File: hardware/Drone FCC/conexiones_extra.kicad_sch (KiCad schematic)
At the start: 4 parts, among them J1 UARTs externo x 3, J1001 SPI externo, J1003 I2C externo x2, J1005 5V y 3V3 x 2

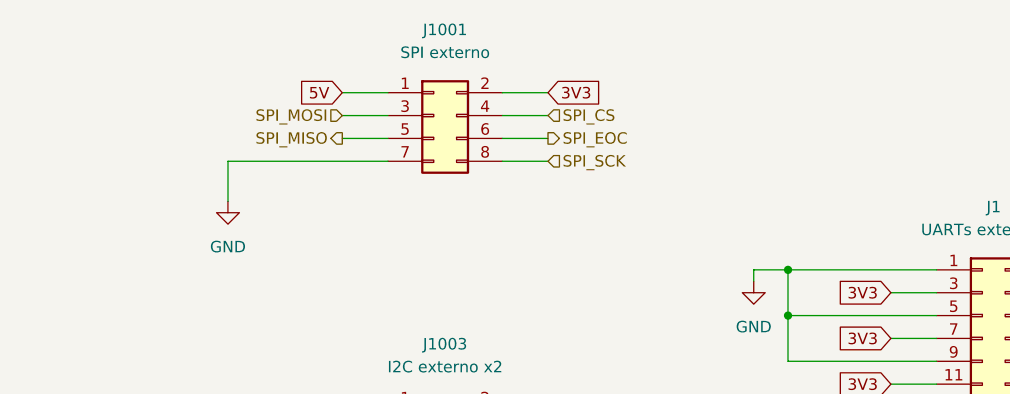
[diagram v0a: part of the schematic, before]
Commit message: add series resistor SPI buses
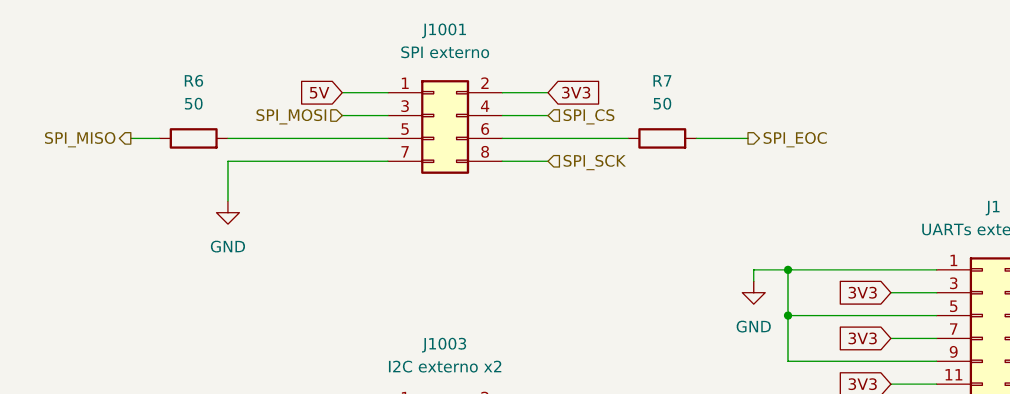
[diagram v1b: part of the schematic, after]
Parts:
- added R6, R7: 50, Resistor_SMD:R_0402_1005Metric_Pad0.72x0.64mm_HandSolder, symbol Device:R
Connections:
- net SPI_EOC: now also R7.2; no longer J1001.6 (Pin_6)
- net SPI_MISO: now also R6.1; no longer J1001.5 (Pin_5)
- new net: J1001.5 (Pin_5), R6.2
- new net: J1001.6 (Pin_6), R7.1
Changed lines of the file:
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@@
     (stroke (width 0) (type default) (color 0 0 0 0))
   )
-  (wire (pts (xy 52.07 35.56) (xy 57.15 35.56))
+  (wire (pts (xy 39.37 35.56) (xy 57.15 35.56))
     (stroke (width 0) (type default) (color 0 0 0 0))
   )
@@
     (stroke (width 0) (type default) (color 0 0 0 0))
   )
+  (wire (pts (xy 91.44 35.56) (xy 97.155 35.56))
+    (stroke (width 0) (type default) (color 0 0 0 0))
+  )
   (wire (pts (xy 57.15 33.02) (xy 52.07 33.02))
     (stroke (width 0) (type default) (color 0 0 0 0))
@@
     (stroke (width 0) (type default) (color 0 0 0 0))
   )
-  (wire (pts (xy 69.85 35.56) (xy 74.93 35.56))
-    (stroke (width 0) (type default) (color 0 0 0 0))
-  )
   (wire (pts (xy 69.85 75.565) (xy 78.74 75.565))
     (stroke (width 0) (type default) (color 0 0 0 0))
   )
+  (wire (pts (xy 69.85 35.56) (xy 83.82 35.56))
+    (stroke (width 0) (type default) (color 0 0 0 0))
+  )
   (wire (pts (xy 101.6 55.245) (xy 118.11 55.245))
     (stroke (width 0) (type default) (color 0 0 0 0))
@@
     (stroke (width 0) (type default) (color 0 0 0 0))
   )
+  (wire (pts (xy 28.575 35.56) (xy 31.75 35.56))
+    (stroke (width 0) (type default) (color 0 0 0 0))
+  )
   (wire (pts (xy 74.93 38.1) (xy 69.85 38.1))
     (stroke (width 0) (type default) (color 0 0 0 0))
@@
     (effects (font (size 1.27 1.27)) (justify right))
   )
-  (hierarchical_label "SPI_EOC" (shape output) (at 74.93 35.56 0)
+  (hierarchical_label "SPI_EOC" (shape output) (at 97.155 35.56 0)
     (effects (font (size 1.27 1.27)) (justify left))
   )
@@
     (effects (font (size 1.27 1.27)) (justify right))
   )
-  (hierarchical_label "SPI_MISO" (shape output) (at 52.07 35.56 180)
+  (hierarchical_label "SPI_MISO" (shape output) (at 28.575 35.56 180)
     (effects (font (size 1.27 1.27)) (justify right))
   )
@@
     (pin "1")
   )
+  (symbol (lib_id "Device:R") (at 87.63 35.56 90) (unit 1)
+    (in_bom yes) (on_board yes) (fields_autoplaced)
+    (property "Reference" "R7" (id 0) (at 87.63 29.21 90))
+    (property "Value" "50" (id 1) (at 87.63 31.75 90))
+    (property "Footprint" "Resistor_SMD:R_0402_1005Metric_Pad0.72x0.64mm_HandSolder" (id 2) (at 87.63 37.338 90)
+      (effects (font (size 1.27 1.27)) hide)
+    )
+    (property "Datasheet" "~" (id 3) (at 87.63 35.56 0)
+      (effects (font (size 1.27 1.27)) hide)
+    )
+    (pin "1")
+    (pin "2")
+  )
+  (symbol (lib_id "Device:R") (at 35.56 35.56 90) (unit 1)
+    (in_bom yes) (on_board yes) (fields_autoplaced)
+    (property "Reference" "R6" (id 0) (at 35.56 29.21 90))
+    (property "Value" "50" (id 1) (at 35.56 31.75 90))
+    (property "Footprint" "Resistor_SMD:R_0402_1005Metric_Pad0.72x0.64mm_HandSolder" (id 2) (at 35.56 37.338 90)
+      (effects (font (size 1.27 1.27)) hide)
+    )
+    (property "Datasheet" "~" (id 3) (at 35.56 35.56 0)
+      (effects (font (size 1.27 1.27)) hide)
+    )
+    (pin "1")
+    (pin "2")
+  )
   (symbol (lib_id "Connector_Generic:Conn_02x06_Odd_Even") (at 123.19 55.245 0) (unit 1)

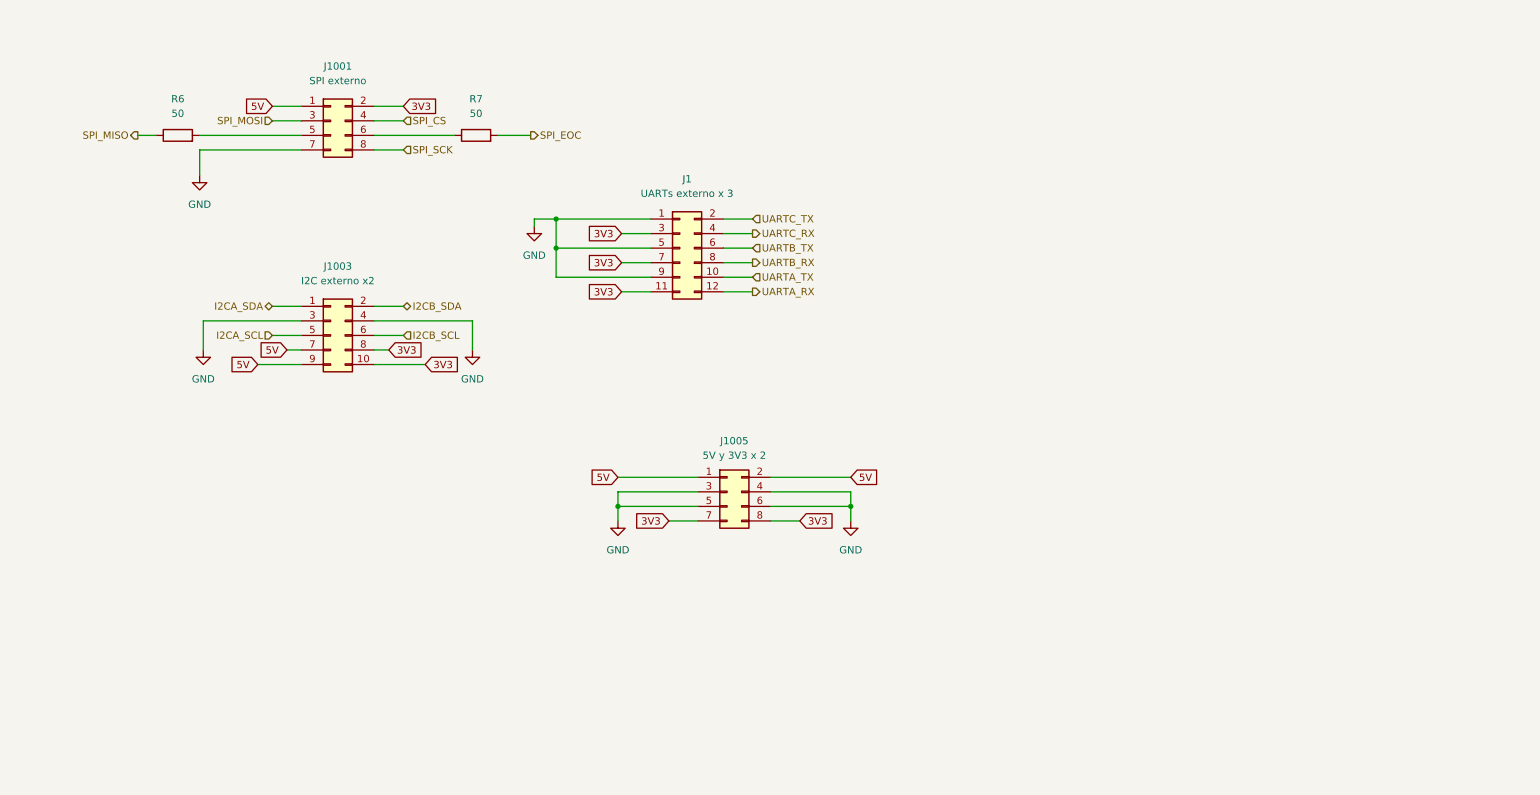
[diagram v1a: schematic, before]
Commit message: add TVS diodes for SPI and ESD capacitors
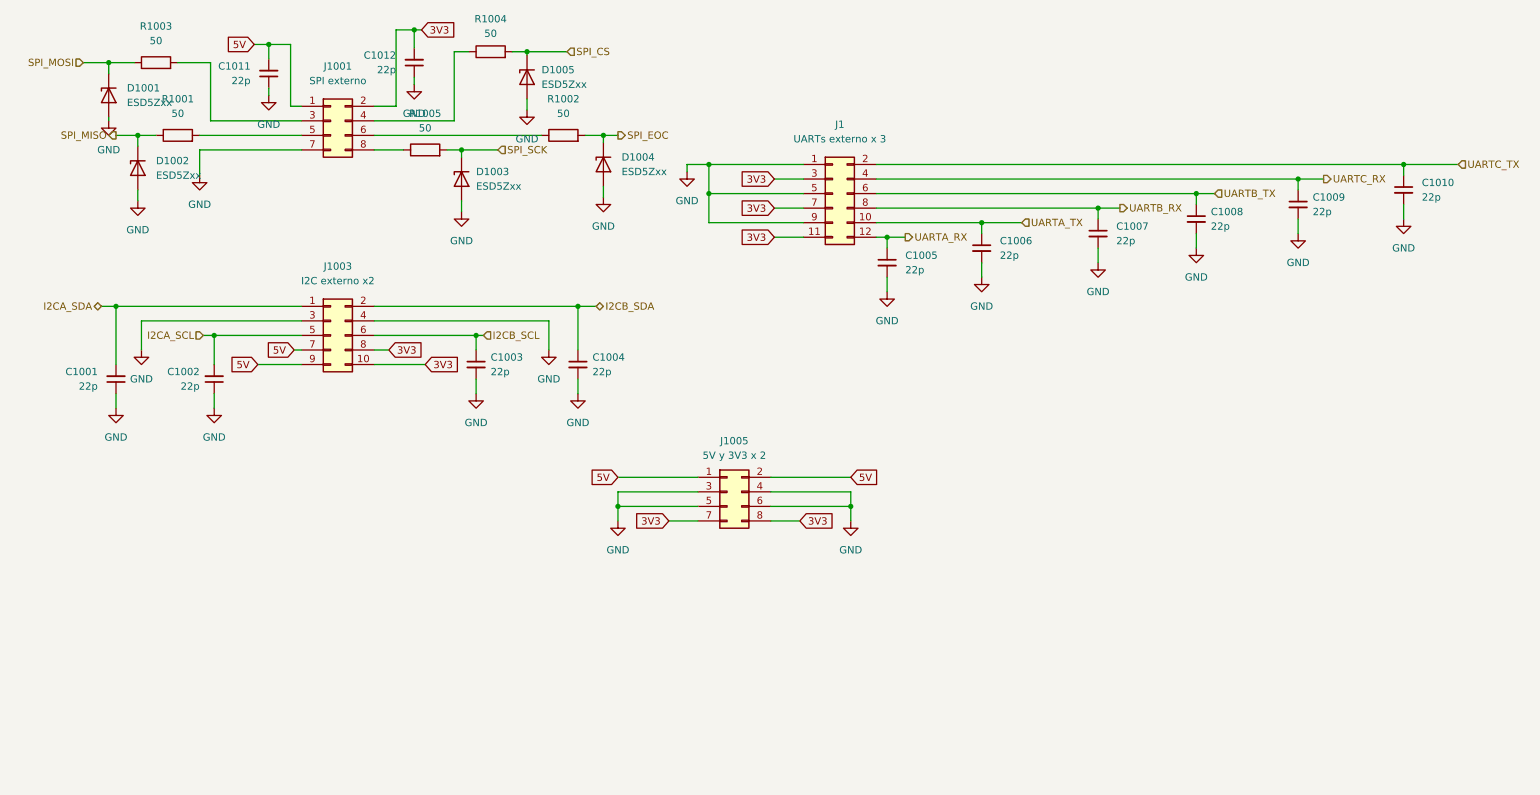
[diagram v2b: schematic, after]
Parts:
- added C1001, C1002, C1003, C1004, C1005, C1006, C1007, C1008, C1009, C1010, C1011, C1012: 22p, Capacitor_SMD:C_0402_1005Metric_Pad0.74x0.62mm_HandSolder, symbol Device:C_Small
- added D1001, D1002, D1003, D1004, D1005: ESD5Zxx, ESDALC6V1-1U2:DIODE_ESDALC6V1-1U2_STM, symbol Diode:ESD5Zxx
- added R1003, R1004, R1005: 50, Resistor_SMD:R_0402_1005Metric_Pad0.72x0.64mm_HandSolder, symbol Device:R
- renumbered R6 to R1001, R7 to R1002
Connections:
- net 3V3: now also C1012.2
- net 5V: now also C1011.2
- net GND: now also C1001.1, C1002.1, C1003.2, C1004.2, C1005.2, C1006.2, C1007.2, C1008.2, C1009.2, C1010.2, C1011.1, C1012.1, D1001.2 (A), D1002.2 (A), D1003.2 (A), D1004.2 (A), D1005.2 (A)
- net I2CA_SCL: now also C1002.2
- net I2CA_SDA: now also C1001.2
- net I2CB_SCL: now also C1003.1
- net I2CB_SDA: now also C1004.1
- net SPI_CS: now also D1005.1 (K), R1004.2; no longer J1001.4 (Pin_4)
- net SPI_EOC: now also D1004.1 (K)
- net SPI_MISO: now also D1002.1 (K)
- net SPI_MOSI: now also D1001.1 (K), R1003.1; no longer J1001.3 (Pin_3)
- net SPI_SCK: now also D1003.1 (K), R1005.2; no longer J1001.8 (Pin_8)
- net UARTA_RX: now also C1005.1
- net UARTA_TX: now also C1006.1
- net UARTB_RX: now also C1007.1
- net UARTB_TX: now also C1008.1
- net UARTC_RX: now also C1009.1
- net UARTC_TX: now also C1010.1
- new net: J1001.3 (Pin_3), R1003.2
- new net: J1001.4 (Pin_4), R1004.1
- new net: J1001.8 (Pin_8), R1005.1
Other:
- moved on the sheet: J1, R1002

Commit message: add TVS diodes for all the dupont pins
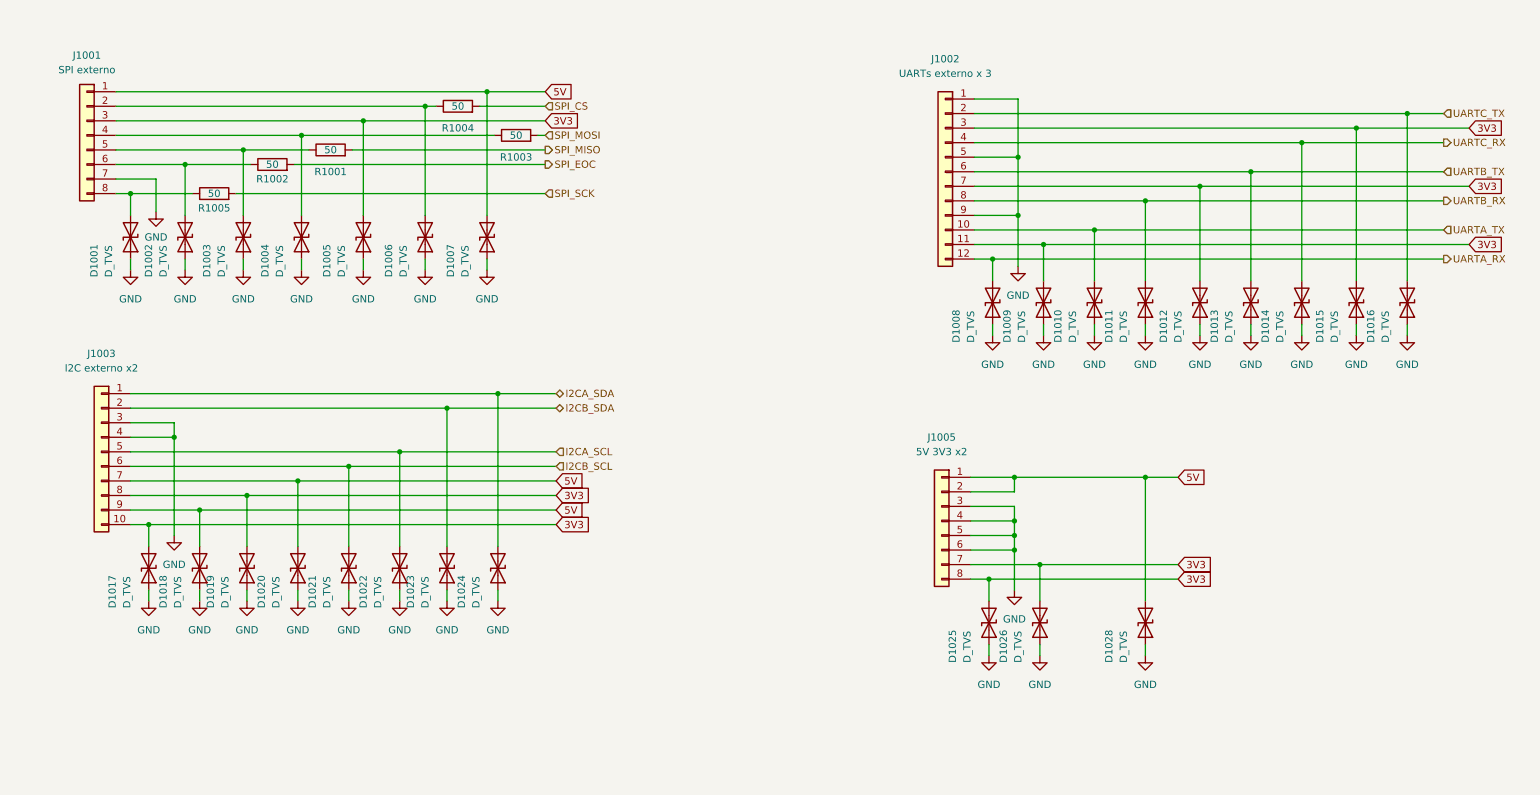
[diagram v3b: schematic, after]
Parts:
- removed C1001, C1002, C1003, C1004, C1005, C1006, C1007, C1008, C1009, C1010, C1011, C1012: 22p, Capacitor_SMD:C_0402_1005Metric_Pad0.74x0.62mm_HandSolder, symbol Device:C_Small
- removed D1001, D1002, D1003, D1004, D1005: ESD5Zxx, ESDALC6V1-1U2:DIODE_ESDALC6V1-1U2_STM, symbol Diode:ESD5Zxx
- removed J1: UARTs externo x 3, Connector_PinHeader_2.54mm:PinHeader_2x06_P2.54mm_Horizontal, symbol Connector_Generic:Conn_02x06_Odd_Even
- removed J1001: SPI externo, Connector_PinHeader_2.54mm:PinHeader_2x04_P2.54mm_Horizontal, symbol Connector_Generic:Conn_02x04_Odd_Even
- removed J1003: I2C externo x2, Connector_PinHeader_2.54mm:PinHeader_2x05_P2.54mm_Horizontal, symbol Connector_Generic:Conn_02x05_Odd_Even
- removed J1005: 5V y 3V3 x 2, Connector_PinHeader_2.54mm:PinHeader_2x04_P2.54mm_Horizontal, symbol Connector_Generic:Conn_02x04_Odd_Even
- added D1001, D1002, D1003, D1004, D1005, D1006, D1007, D1008, D1009, D1010, D1011, D1012, D1013, D1014, D1015, D1016, D1017, D1018, D1019, D1020, D1021, D1022, D1023, D1024, D1025, D1026, D1028: D_TVS, Diode_SMD:D_0402_1005Metric_Pad0.77x0.64mm_HandSolder, symbol Device:D_TVS
- added J1001: SPI externo, Connector_PinHeader_2.54mm:PinHeader_2x04_P2.54mm_Horizontal, symbol Connector_Generic:Conn_01x08
- added J1002: UARTs externo x 3, Connector_PinHeader_2.54mm:PinHeader_2x06_P2.54mm_Horizontal, symbol Connector_Generic:Conn_01x12
- added J1003: I2C externo x2, Connector_PinHeader_2.54mm:PinHeader_2x05_P2.54mm_Horizontal, symbol Connector_Generic:Conn_01x10
- added J1005: 5V 3V3 x2, Connector_PinHeader_2.54mm:PinHeader_2x04_P2.54mm_Horizontal, symbol Connector_Generic:Conn_01x08
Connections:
- net 3V3: now also D1005.2 (A2), D1009.2 (A2), D1012.2 (A2), D1015.2 (A2), D1017.2 (A2), D1019.2 (A2), D1025.2 (A2), D1026.2 (A2), J1001.3 (Pin_3), J1002.11 (Pin_11), J1002.3 (Pin_3), J1002.7 (Pin_7), J1003.10 (Pin_10), J1003.8 (Pin_8), J1005.7 (Pin_7), J1005.8 (Pin_8)
- net 5V: now also D1007.2 (A2), D1018.2 (A2), D1020.2 (A2), D1028.2 (A2), J1001.1 (Pin_1), J1003.7 (Pin_7), J1003.9 (Pin_9), J1005.1 (Pin_1), J1005.2 (Pin_2)
- net GND: now also D1001.1 (A1), D1002.1 (A1), D1003.1 (A1), D1004.1 (A1), D1005.1 (A1), D1006.1 (A1), D1007.1 (A1), D1008.1 (A1), D1009.1 (A1), D1010.1 (A1), D1011.1 (A1), D1012.1 (A1), D1013.1 (A1), D1014.1 (A1), D1015.1 (A1), D1016.1 (A1), D1017.1 (A1), D1018.1 (A1), D1019.1 (A1), D1020.1 (A1), D1021.1 (A1), D1022.1 (A1), D1023.1 (A1), D1024.1 (A1), D1025.1 (A1), D1026.1 (A1), D1028.1 (A1), J1001.7 (Pin_7), J1002.1 (Pin_1), J1002.5 (Pin_5), J1002.9 (Pin_9), J1003.3 (Pin_3), J1003.4 (Pin_4), J1005.3 (Pin_3), J1005.4 (Pin_4), J1005.5 (Pin_5), J1005.6 (Pin_6)
- net I2CA_SCL: now also D1022.2 (A2), J1003.5 (Pin_5)
- net I2CA_SDA: now also D1024.2 (A2), J1003.1 (Pin_1)
- net I2CB_SCL: now also D1021.2 (A2), J1003.6 (Pin_6)
- net I2CB_SDA: now also D1023.2 (A2), J1003.2 (Pin_2)
- net SPI_MISO: now also R1001.2; no longer R1001.1
- net SPI_MOSI: now also R1003.2; no longer R1003.1
- net UARTA_RX: now also D1008.2 (A2), J1002.12 (Pin_12)
- net UARTA_TX: now also D1010.2 (A2), J1002.10 (Pin_10)
- net UARTB_RX: now also D1011.2 (A2), J1002.8 (Pin_8)
- net UARTB_TX: now also D1013.2 (A2), J1002.6 (Pin_6)
- net UARTC_RX: now also D1014.2 (A2), J1002.4 (Pin_4)
- net UARTC_TX: now also D1016.2 (A2), J1002.2 (Pin_2)
- net at R1004.1: now also D1006.2 (A2), J1001.2 (Pin_2)
- net at R1002.1: now also D1002.2 (A2), J1001.6 (Pin_6)
- net at R1005.1: now also D1001.2 (A2), J1001.8 (Pin_8)
- new net: D1003.2 (A2), J1001.5 (Pin_5), R1001.1
- new net: D1004.2 (A2), J1001.4 (Pin_4), R1003.1
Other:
- moved on the sheet: R1001, R1002, R1003, R1004, R1005
